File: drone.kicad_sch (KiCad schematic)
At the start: 1 part, among them J4 217175-0001

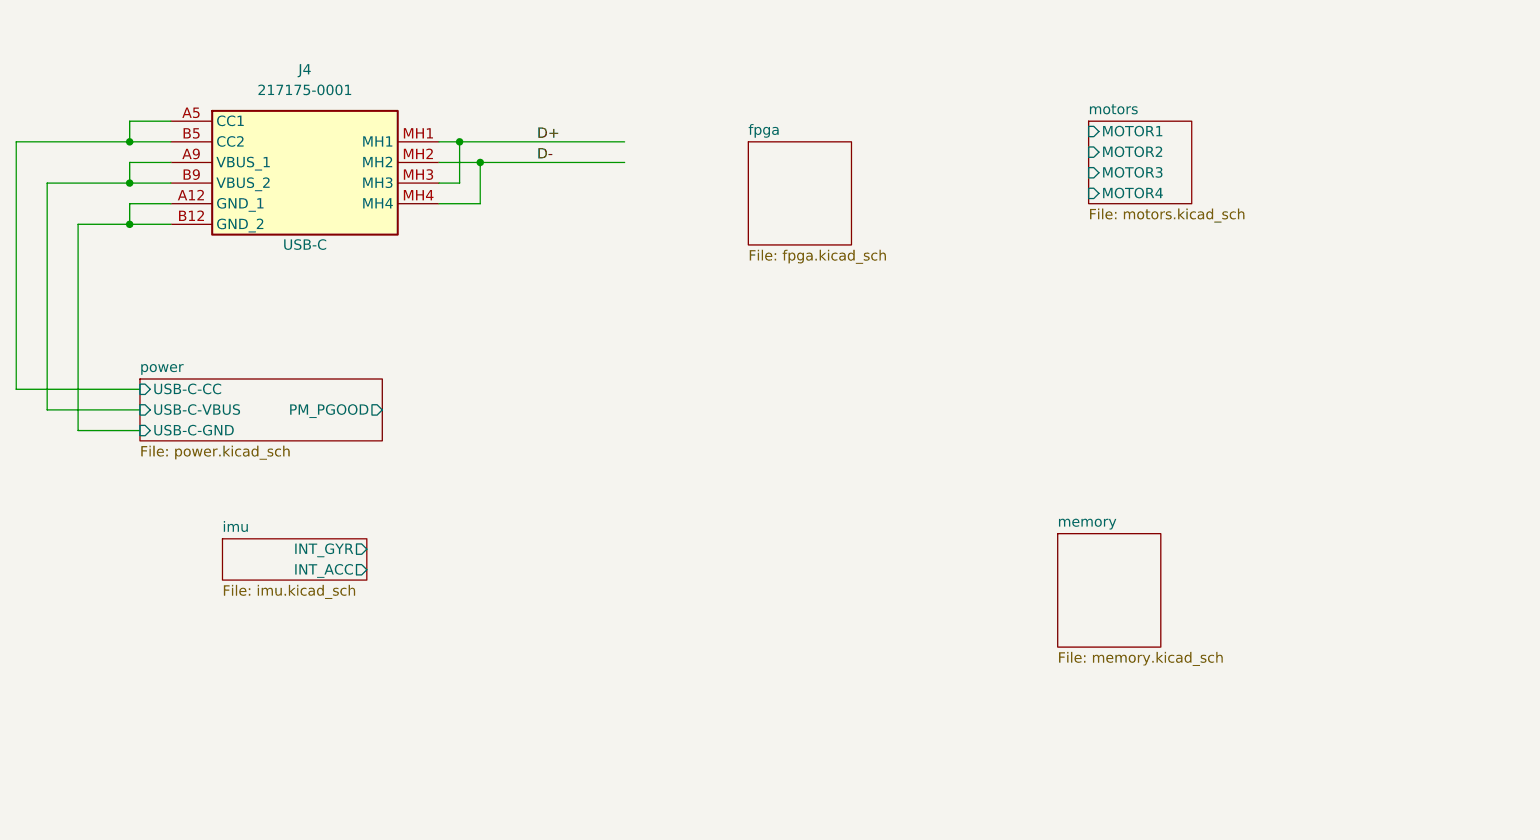
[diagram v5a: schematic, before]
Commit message: Replacing global power labels with hierarchical pins
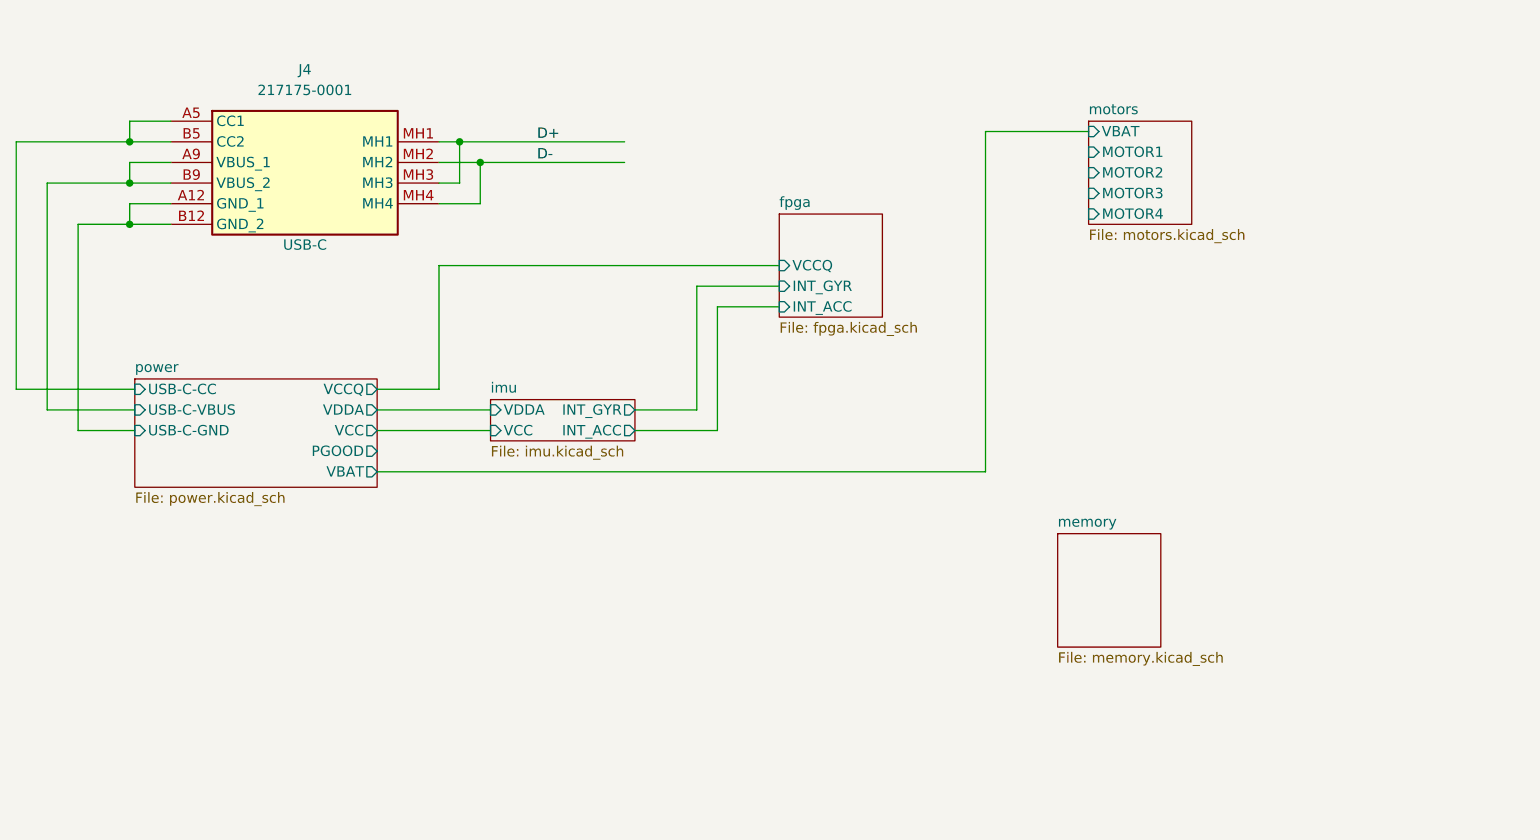
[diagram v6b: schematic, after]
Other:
- sheet fpga ports: added INT_ACC, INT_GYR, VCCQ; removed none
- sheet imu ports: added VCC, VDDA; removed none
- sheet motors ports: added VBAT; removed none
- sheet power ports: added PGOOD, VBAT, VCC, VCCQ, VDDA; removed PM_PGOOD
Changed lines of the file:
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@@
     (stroke (width 0) (type default))
   )
-  (wire (pts (xy 21.59 66.04) (xy 33.02 66.04))
+  (wire (pts (xy 62.23 63.5) (xy 69.85 63.5))
+    (stroke (width 0) (type default))
+  )
+  (wire (pts (xy 21.59 66.04) (xy 32.385 66.04))
+    (stroke (width 0) (type default))
+  )
+  (wire (pts (xy 137.16 73.66) (xy 137.16 31.75))
     (stroke (width 0) (type default))
   )
@@
     (stroke (width 0) (type default))
   )
+  (wire (pts (xy 104.14 68.58) (xy 104.14 53.34))
+    (stroke (width 0) (type default))
+  )
+  (wire (pts (xy 93.98 68.58) (xy 104.14 68.58))
+    (stroke (width 0) (type default))
+  )
+  (wire (pts (xy 69.85 48.26) (xy 111.76 48.26))
+    (stroke (width 0) (type default))
+  )
   (wire (pts (xy 21.59 38.1) (xy 21.59 66.04))
     (stroke (width 0) (type default))
   )
+  (wire (pts (xy 137.16 31.75) (xy 149.86 31.75))
+    (stroke (width 0) (type default))
+  )
+  (wire (pts (xy 62.23 66.04) (xy 76.2 66.04))
+    (stroke (width 0) (type default))
+  )
   (wire (pts (xy 17.78 33.02) (xy 31.75 33.02))
     (stroke (width 0) (type default))
@@
     (stroke (width 0) (type default))
   )
+  (wire (pts (xy 101.6 50.8) (xy 111.76 50.8))
+    (stroke (width 0) (type default))
+  )
+  (wire (pts (xy 62.23 68.58) (xy 76.2 68.58))
+    (stroke (width 0) (type default))
+  )
   (wire (pts (xy 69.85 38.1) (xy 72.39 38.1))
     (stroke (width 0) (type default))
@@
     (stroke (width 0) (type default))
   )
-  (wire (pts (xy 25.4 68.58) (xy 33.02 68.58))
+  (wire (pts (xy 25.4 68.58) (xy 32.385 68.58))
     (stroke (width 0) (type default))
   )
@@
     (stroke (width 0) (type default))
   )
-  (wire (pts (xy 17.78 63.5) (xy 33.02 63.5))
+  (wire (pts (xy 17.78 63.5) (xy 32.385 63.5))
+    (stroke (width 0) (type default))
+  )
+  (wire (pts (xy 62.23 73.66) (xy 137.16 73.66))
+    (stroke (width 0) (type default))
+  )
+  (wire (pts (xy 93.98 66.04) (xy 101.6 66.04))
     (stroke (width 0) (type default))
   )
@@
     (stroke (width 0) (type default))
   )
+  (wire (pts (xy 101.6 66.04) (xy 101.6 50.8))
+    (stroke (width 0) (type default))
+  )
   (wire (pts (xy 74.93 40.64) (xy 74.93 35.56))
     (stroke (width 0) (type default))
@@
     (stroke (width 0) (type default))
   )
+  (wire (pts (xy 104.14 53.34) (xy 111.76 53.34))
+    (stroke (width 0) (type default))
+  )
   (wire (pts (xy 36.83 30.48) (xy 31.75 30.48))
     (stroke (width 0) (type default))
@@
   )
   (wire (pts (xy 74.93 35.56) (xy 92.71 35.56))
+    (stroke (width 0) (type default))
+  )
+  (wire (pts (xy 69.85 63.5) (xy 69.85 48.26))
     (stroke (width 0) (type default))
   )
@@
     )
   )
-  (sheet (at 149.86 30.48) (size 12.7 10.16) (fields_autoplaced)
+  (sheet (at 149.86 30.48) (size 12.7 12.7) (fields_autoplaced)
     (stroke (width 0.1524) (type solid))
     (fill (color 0 0 0 0.0000))
@@
       (effects (font (size 1.27 1.27)) (justify left bottom))
     )
-    (property "Sheetfile" "motors.kicad_sch" (at 149.86 41.2246 0)
-      (effects (font (size 1.27 1.27)) (justify left top))
-    )
-    (pin "MOTOR3" input (at 149.86 36.83 180)
-      (effects (font (size 1.27 1.27)) (justify left))
-    )
-    (pin "MOTOR2" input (at 149.86 34.29 180)
-      (effects (font (size 1.27 1.27)) (justify left))
-    )
-    (pin "MOTOR1" input (at 149.86 31.75 180)
-      (effects (font (size 1.27 1.27)) (justify left))
-    )
-    (pin "MOTOR4" input (at 149.86 39.37 180)
+    (property "Sheetfile" "motors.kicad_sch" (at 149.86 43.7646 0)
+      (effects (font (size 1.27 1.27)) (justify left top))
+    )
+    (pin "MOTOR3" input (at 149.86 39.37 180)
+      (effects (font (size 1.27 1.27)) (justify left))
+    )
+    (pin "MOTOR2" input (at 149.86 36.83 180)
+      (effects (font (size 1.27 1.27)) (justify left))
+    )
+    (pin "MOTOR1" input (at 149.86 34.29 180)
+      (effects (font (size 1.27 1.27)) (justify left))
+    )
+    (pin "MOTOR4" input (at 149.86 41.91 180)
+      (effects (font (size 1.27 1.27)) (justify left))
+    )
+    (pin "VBAT" input (at 149.86 31.75 180)
       (effects (font (size 1.27 1.27)) (justify left))
     )
@@
     )
   )
-  (sheet (at 107.95 33.02) (size 12.7 12.7) (fields_autoplaced)
-    (stroke (width 0.1524) (type solid))
-    (fill (color 0 0 0 0.0000))
-    (property "Sheetname" "fpga" (at 107.95 32.3084 0)
-      (effects (font (size 1.27 1.27)) (justify left bottom))
-    )
-    (property "Sheetfile" "fpga.kicad_sch" (at 107.95 46.3046 0)
-      (effects (font (size 1.27 1.27)) (justify left top))
+  (sheet (at 111.76 41.91) (size 12.7 12.7) (fields_autoplaced)
+    (stroke (width 0.1524) (type solid))
+    (fill (color 0 0 0 0.0000))
+    (property "Sheetname" "fpga" (at 111.76 41.1984 0)
+      (effects (font (size 1.27 1.27)) (justify left bottom))
+    )
+    (property "Sheetfile" "fpga.kicad_sch" (at 111.76 55.1946 0)
+      (effects (font (size 1.27 1.27)) (justify left top))
+    )
+    (pin "VCCQ" input (at 111.76 48.26 180)
+      (effects (font (size 1.27 1.27)) (justify left))
+    )
+    (pin "INT_ACC" input (at 111.76 53.34 180)
+      (effects (font (size 1.27 1.27)) (justify left))
+    )
+    (pin "INT_GYR" input (at 111.76 50.8 180)
+      (effects (font (size 1.27 1.27)) (justify left))
     )
     (instances
@@
     )
   )
-  (sheet (at 43.18 81.915) (size 17.78 5.08) (fields_autoplaced)
-    (stroke (width 0.1524) (type solid))
-    (fill (color 0 0 0 0.0000))
-    (property "Sheetname" "imu" (at 43.18 81.2034 0)
-      (effects (font (size 1.27 1.27)) (justify left bottom))
-    )
-    (property "Sheetfile" "imu.kicad_sch" (at 43.18 87.5796 0)
-      (effects (font (size 1.27 1.27)) (justify left top))
-    )
-    (pin "INT_GYR" output (at 60.96 83.185 0)
-      (effects (font (size 1.27 1.27)) (justify right))
-    )
-    (pin "INT_ACC" output (at 60.96 85.725 0)
-      (effects (font (size 1.27 1.27)) (justify right))
+  (sheet (at 76.2 64.77) (size 17.78 5.08) (fields_autoplaced)
+    (stroke (width 0.1524) (type solid))
+    (fill (color 0 0 0 0.0000))
+    (property "Sheetname" "imu" (at 76.2 64.0584 0)
+      (effects (font (size 1.27 1.27)) (justify left bottom))
+    )
+    (property "Sheetfile" "imu.kicad_sch" (at 76.2 70.4346 0)
+      (effects (font (size 1.27 1.27)) (justify left top))
+    )
+    (pin "INT_GYR" output (at 93.98 66.04 0)
+      (effects (font (size 1.27 1.27)) (justify right))
+    )
+    (pin "INT_ACC" output (at 93.98 68.58 0)
+      (effects (font (size 1.27 1.27)) (justify right))
+    )
+    (pin "VDDA" input (at 76.2 66.04 180)
+      (effects (font (size 1.27 1.27)) (justify left))
+    )
+    (pin "VCC" input (at 76.2 68.58 180)
+      (effects (font (size 1.27 1.27)) (justify left))
     )
     (instances
@@
     )
   )
-  (sheet (at 33.02 62.23) (size 29.845 7.62) (fields_autoplaced)
-    (stroke (width 0.1524) (type solid))
-    (fill (color 0 0 0 0.0000))
-    (property "Sheetname" "power" (at 33.02 61.5184 0)
-      (effects (font (size 1.27 1.27)) (justify left bottom))
-    )
-    (property "Sheetfile" "power.kicad_sch" (at 33.02 70.4346 0)
-      (effects (font (size 1.27 1.27)) (justify left top))
-    )
-    (pin "PM_PGOOD" output (at 62.865 66.04 0)
-      (effects (font (size 1.27 1.27)) (justify right))
-    )
-    (pin "USB-C-CC" input (at 33.02 63.5 180)
-      (effects (font (size 1.27 1.27)) (justify left))
-    )
-    (pin "USB-C-VBUS" input (at 33.02 66.04 180)
-      (effects (font (size 1.27 1.27)) (justify left))
-    )
-    (pin "USB-C-GND" input (at 33.02 68.58 180)
-      (effects (font (size 1.27 1.27)) (justify left))
-    )
-    (instances
+  (sheet (at 32.385 62.23) (size 29.845 13.335) (fields_autoplaced)
+    (stroke (width 0.1524) (type solid))
+    (fill (color 0 0 0 0.0000))
+    (property "Sheetname" "power" (at 32.385 61.5184 0)
+      (effects (font (size 1.27 1.27)) (justify left bottom))
+    )
+    (property "Sheetfile" "power.kicad_sch" (at 32.385 76.1496 0)
+      (effects (font (size 1.27 1.27)) (justify left top))
+    )
+    (pin "PGOOD" output (at 62.23 71.12 0)
+      (effects (font (size 1.27 1.27)) (justify right))
+    )
+    (pin "USB-C-CC" input (at 32.385 63.5 180)
+      (effects (font (size 1.27 1.27)) (justify left))
+    )
+    (pin "USB-C-VBUS" input (at 32.385 66.04 180)
+      (effects (font (size 1.27 1.27)) (justify left))
+    )
+    (pin "USB-C-GND" input (at 32.385 68.58 180)
+      (effects (font (size 1.27 1.27)) (justify left))
+    )
+    (pin "VCCQ" output (at 62.23 63.5 0)
+      (effects (font (size 1.27 1.27)) (justify right))
+    )
+    (pin "VCC" output (at 62.23 68.58 0)
+      (effects (font (size 1.27 1.27)) (justify right))
+    )
+    (pin "VDDA" output (at 62.23 66.04 0)
+      (effects (font (size 1.27 1.27)) (justify right))
+    )
+    (pin "VBAT" output (at 62.23 73.66 0)
+      (effects (font (size 1.27 1.27)) (justify right))
+    )
+    (instances

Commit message: Gathering memory components
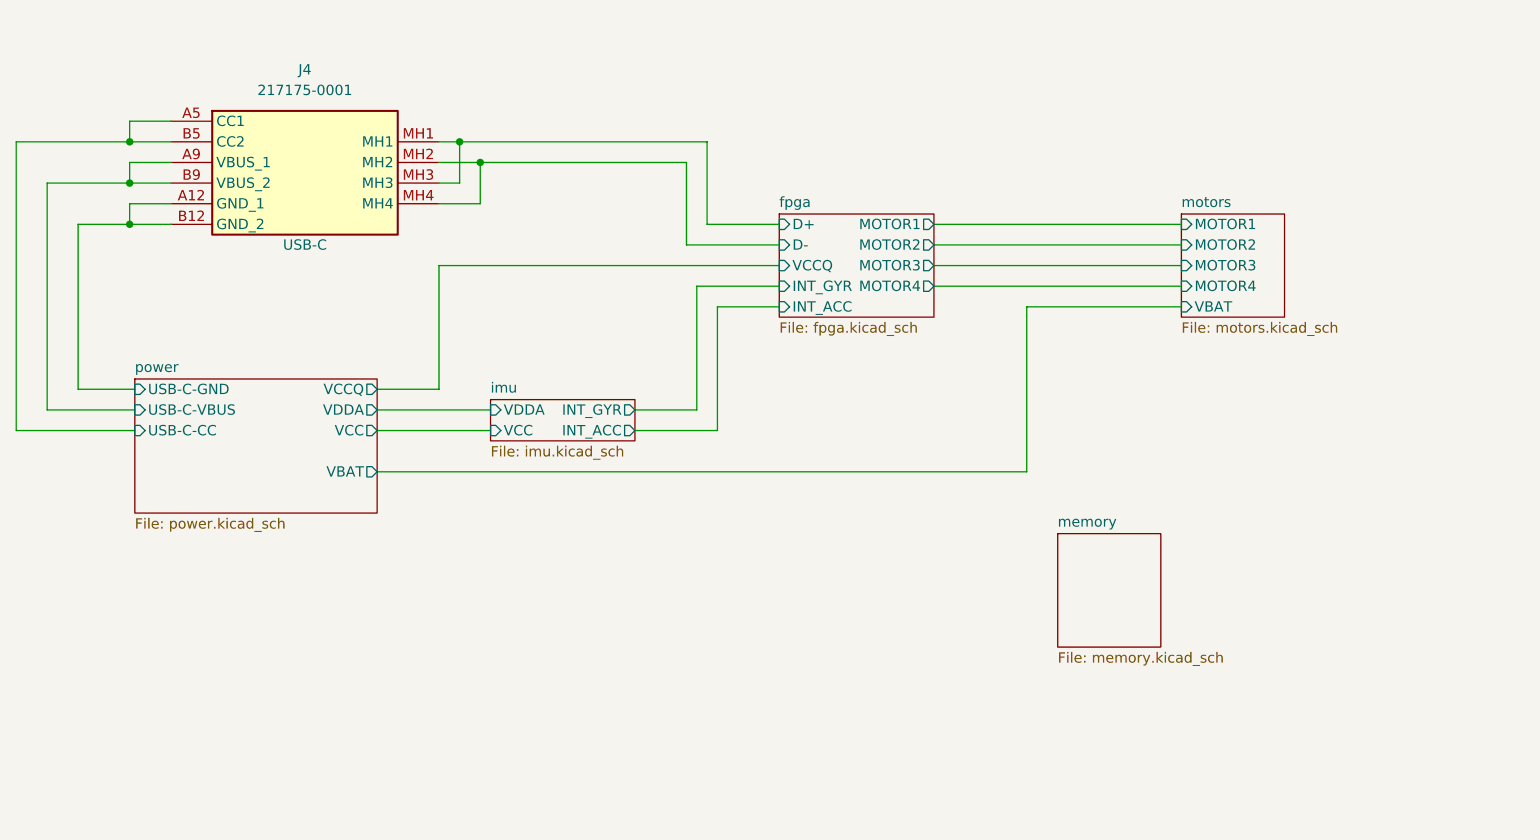
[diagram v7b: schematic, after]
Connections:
- net D+ renamed fpga/D+
- net D- renamed fpga/D-
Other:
- sheet fpga ports: added D+, D-, MOTOR1, MOTOR2, MOTOR3, MOTOR4; removed none
- sheet power ports: added none; removed PGOOD

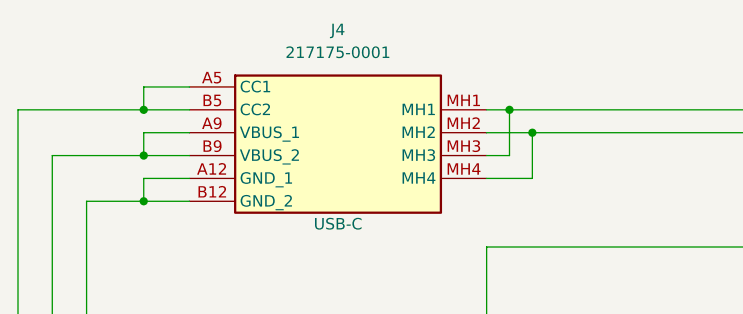
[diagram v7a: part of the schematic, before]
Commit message: Updated KiCad Version of files
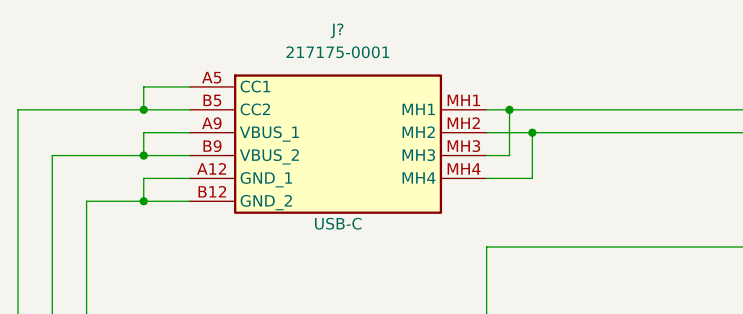
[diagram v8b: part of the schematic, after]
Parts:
- renumbered J4 to J?
